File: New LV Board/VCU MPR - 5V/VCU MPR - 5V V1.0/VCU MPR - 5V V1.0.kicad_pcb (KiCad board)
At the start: 2 copper layers, 46 x 51.3 mm, 9 parts, among them J1 Conn_01x12, K1 ALF1PF12, P1 PH1-20-UA, P2 PH1-20-UA, U1 LT1117-5.0

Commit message: Changed some labels
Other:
- board text added: "VCU MPR - 1 GLV + - (2 - 4) GLV VCU + - (5 - 7)"
- board text removed: "VCU MPR - 1 GLV + - (2 - 4) VCU + - (5 - 7)"
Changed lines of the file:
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@@
 		)
 	)
-	(gr_text "VCU MPR - 1\nGLV + - (2 - 4)\nVCU + - (5 - 7)"
+	(gr_text "VCU MPR - 1\nGLV + - (2 - 4)\nGLV VCU + - (5 - 7)"
 		(at 99.3394 73.826833 0)
 		(layer "F.SilkS")

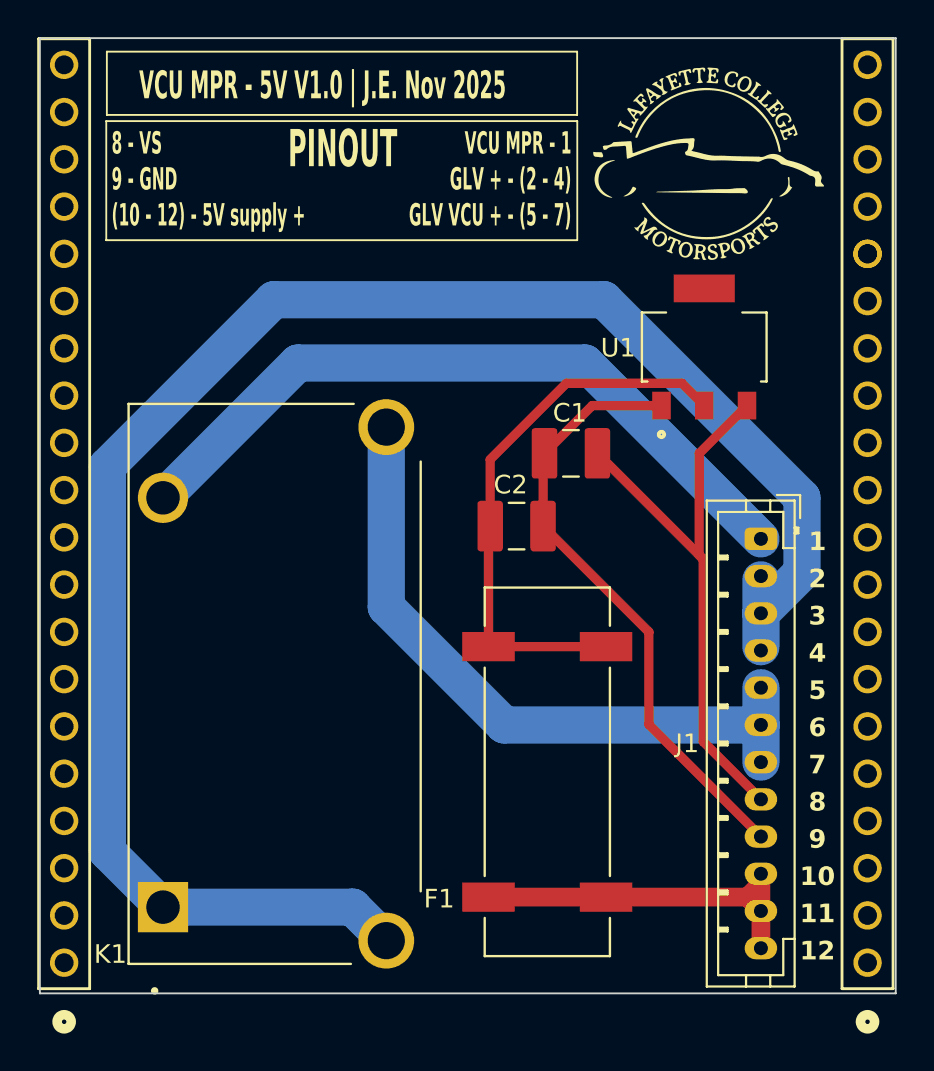
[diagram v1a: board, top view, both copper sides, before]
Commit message: Changed Board Width
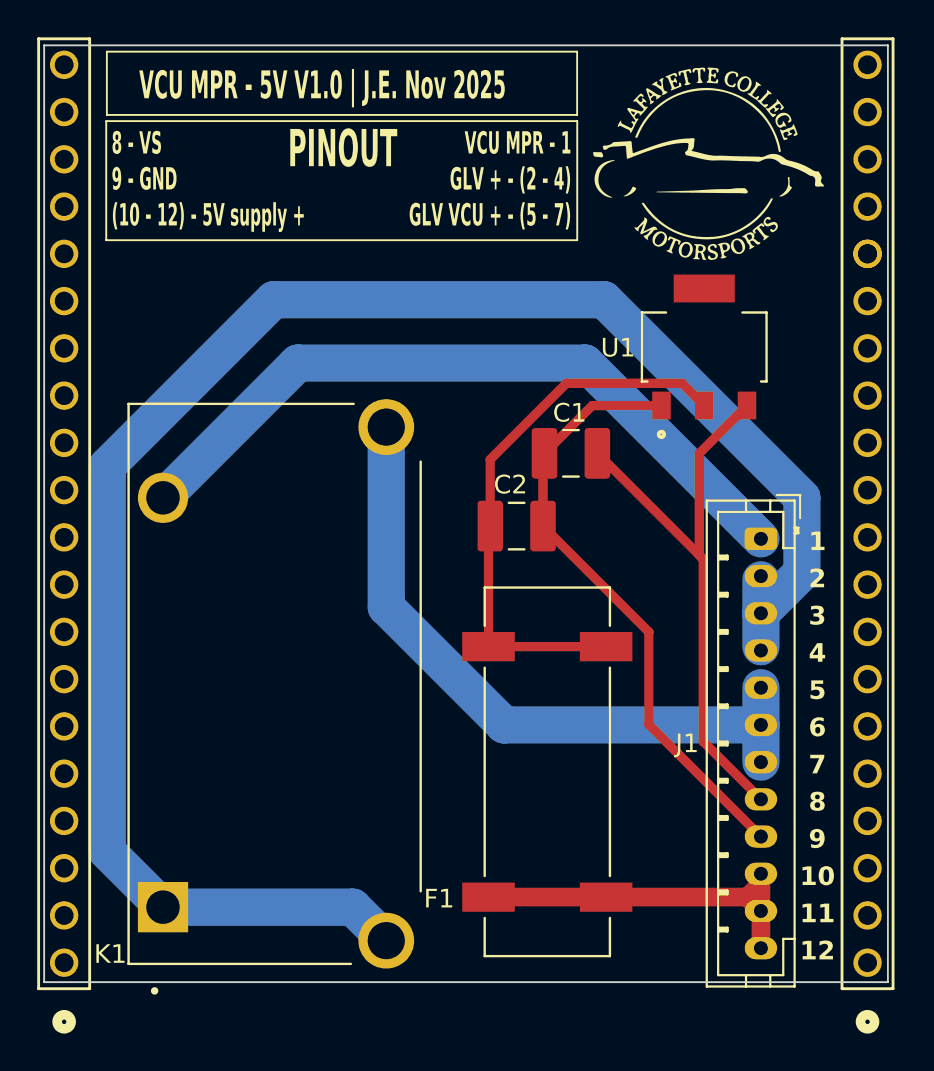
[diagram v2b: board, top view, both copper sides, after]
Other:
- board size 46 x 51.3 mm -> 45.3 x 50.3 mm
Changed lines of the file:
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@@
 	)
 	(gr_rect
-		(start 70.77082 63.613139)
-		(end 116.77022 114.954339)
+		(start 71 64)
+		(end 116.35 114.35)
 		(stroke
 			(width 0.1)
